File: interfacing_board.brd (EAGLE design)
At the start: 85.1 x 74.6 mm, 46 parts, among them IC1 MAX3096CSE, X1 87758-3816, X2 87758-3816

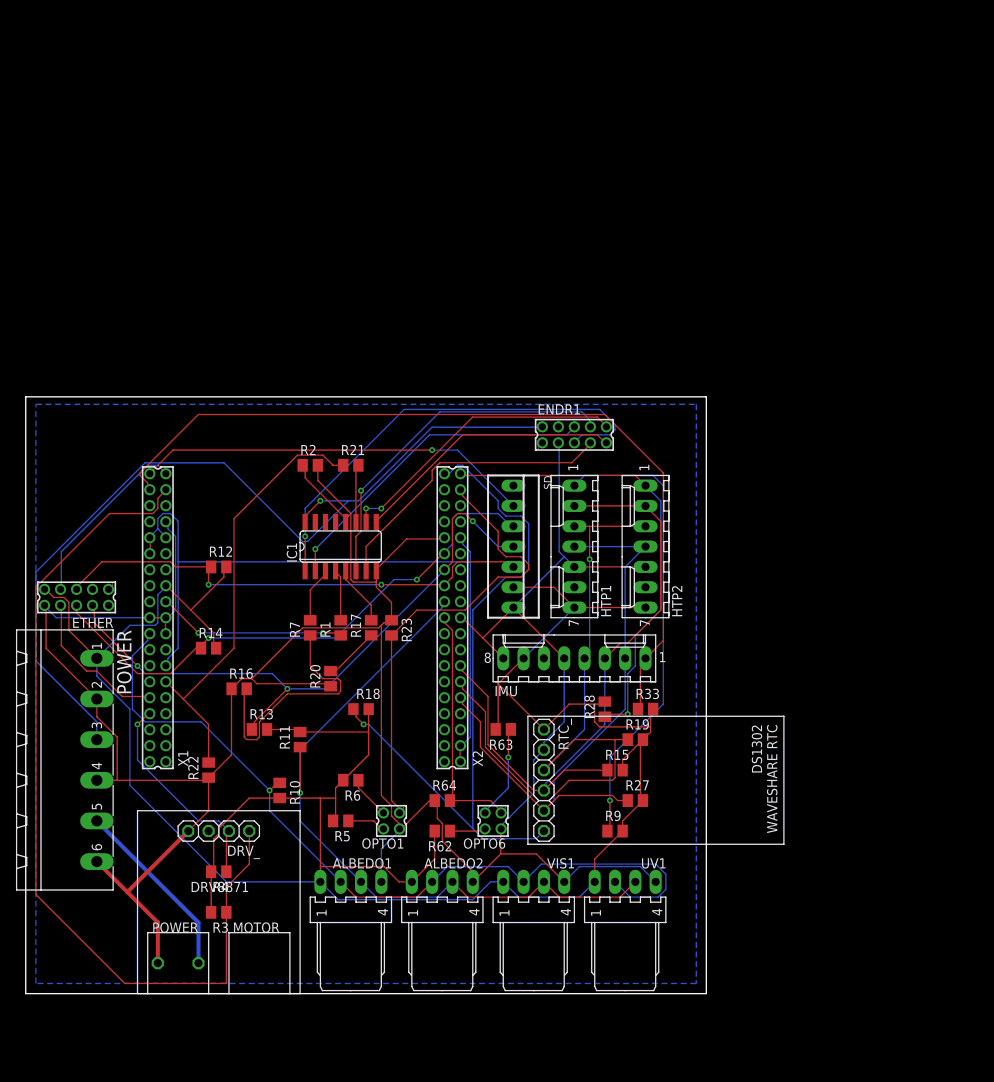
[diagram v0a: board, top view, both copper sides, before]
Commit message: Nucleo and ethernet module library components added. Implemented in schematics and PCB. Redesign of the PCB, errors removal.
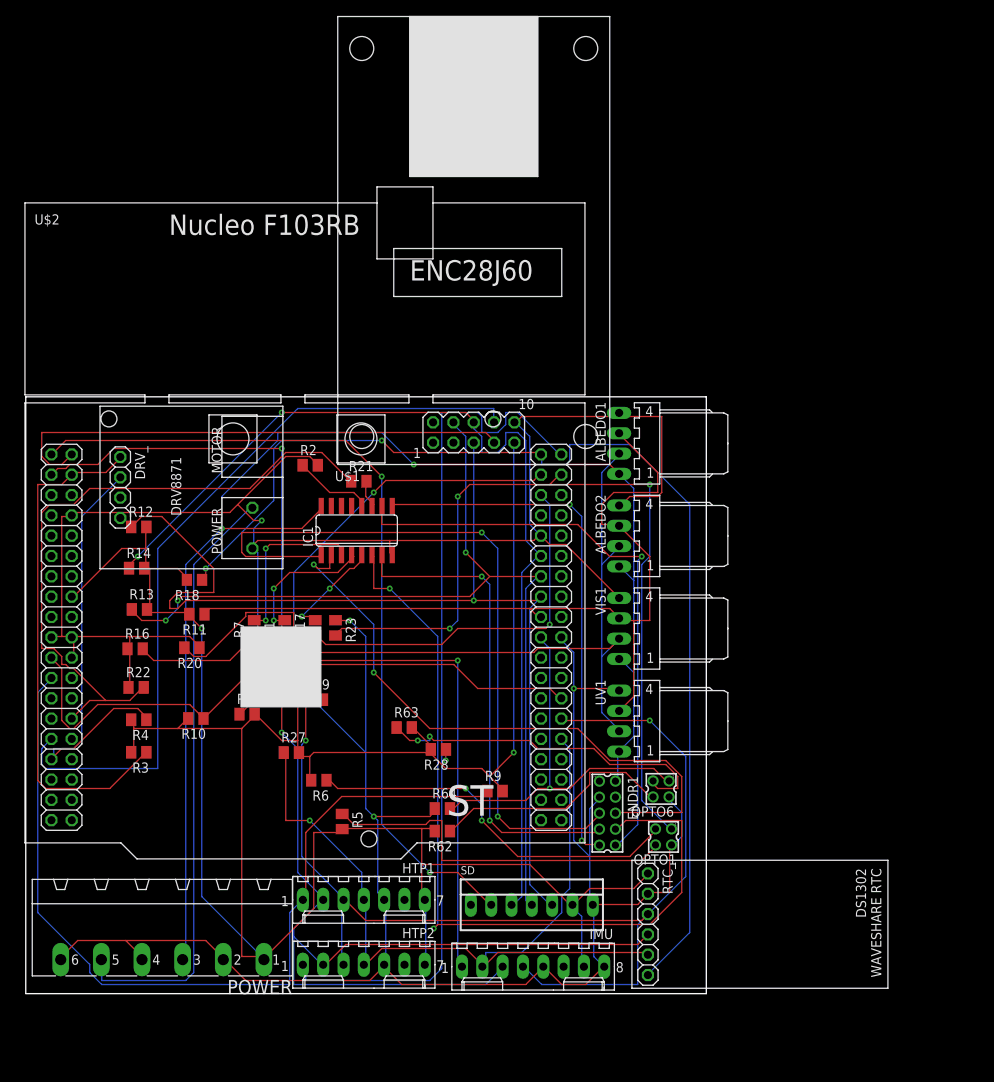
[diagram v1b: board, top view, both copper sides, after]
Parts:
- removed ETHER: 332-10, con-garry:332-10
- removed X1, X2: 87758-3816, con-molex:87758-3816
- added U$1: ETHERNET, customy:ETHERNET
- added U$2: NUCLEOF103, customy:NUCLEO
- moved ALBEDO1 64.3 mm to (74.2, 91.6), turned to 270 degrees
- moved HTP2 63.0 mm to (42.3, 26.5), turned to 180 degrees
- moved HTP1 51.4 mm to (42.3, 34.6), turned to 180 degrees
- moved ALBEDO2 48.6 mm to (74.2, 80.1), turned to 270 degrees
- moved ENDR1 47.5 mm to (72.7, 45.4), turned to 270 degrees
- moved R15 46.5 mm to (27.7, 57.8)
- moved R33 45.2 mm to (32.5, 62.4)
- moved SD 44.8 mm to (63.3, 34.0), turned to 0 degrees
- moved R27 43.4 mm to (33.2, 53.0)
- moved DRV_ 41.6 mm to (11.8, 83.6), turned to 270 degrees
- moved R19 40.3 mm to (36.2, 59.6)
- moved IMU 38.9 mm to (63.4, 26.2), turned to 180 degrees
- moved OPTO1 34.1 mm to (79.7, 42.5)
- moved VIS1 33.4 mm to (74.2, 68.5), turned to 270 degrees
- moved R18 26.4 mm to (21.1, 74.6), turned to 180 degrees
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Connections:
- removed net ADC12_IN8: X1.5
- removed net ADC12_IN9: X1.3
- removed net AGND: X2.7
- removed net AVDD: X2.32
- removed net BOOT0: X1.32
- removed net E5V: X1.33
- removed net INT: ETHER.2
- removed net IOREF: X1.27
- removed net NC: X1.13, X1.28, X1.29, X1.30, X2.1, X2.29, X2.3
- removed net PA1: X1.9
- removed net PA10: X2.6
- removed net PA11: X2.25
- removed net PA12: X2.27
- removed net PA13: X1.26
- removed net PA14: X1.24
- removed net PA15: X1.22
- removed net PA2: X2.4
- removed net PA3: X2.2
- removed net PA8: X2.16
- removed net PA9: X2.18
- removed net PB1: X2.15
- removed net PB10: X2.14
- removed net PB11: X2.21
- removed net PB12: X2.23
- removed net PB2: X2.17
- removed net PB3: X2.8
- removed net PB4: X2.12
- removed net PB5: X2.10
- removed net PB8: X2.36
- removed net PB9: X2.34
- removed net PC0: X1.1
- removed net PC13: X1.16
- removed net PC14: X1.14
- removed net PC15: X1.12
- removed net PC2: X1.4
- removed net PC3: X1.2
- removed net PC4: X2.5
- removed net PC5: X2.33
- removed net RESET: X1.25
- removed net SPI1_NSS: X1.7
- removed net U5V: X2.31
- removed net VBAT: X1.6
- removed net VDD: X1.34
- removed net VIN: X1.15
- new net ETH_INT: U$1.INT
- new net N$17: U$2.PC5
- new net N$20: U$2.PC4
- new net N$21: U$2.PC3
- new net N$22: U$2.PC2
- new net N$23: U$2.PC1
- new net N$24: U$2.PC0
- new net N$28: U$2.RESET
- new net N$29: U$2.BOOT0
- new net N$3: U$2.PC15
- new net N$30: U$2.IOREF
- new net N$34: U$2.PA1
- new net N$35: U$2.PA2
- new net N$36: U$2.PA3
- new net N$37: U$2.PA4
- new net N$4: U$1.WOL
- new net N$41: U$2.PA8
- new net N$42: U$2.PA9
- new net N$43: U$2.PA10
- new net N$44: U$2.PA11
- new net N$45: U$2.PA12
- new net N$46: U$2.PA13
- new net N$47: U$2.PA14
- new net N$48: U$2.PA15
- new net N$49: U$2.PB0
- new net N$5: U$2.PC14
- new net N$50: U$2.PB1
- new net N$51: U$2.PB2
- new net N$52: U$2.PB3
- new net N$53: U$2.PB4
- new net N$54: U$2.PB5
- new net N$59: U$2.PB10
- new net N$60: U$2.PB11
- new net N$61: U$2.PB12
- net +5V: no longer X1.21
- net 3.3V: now also U$1.VCC, U$2.3V3; no longer ALBEDO1.1, ALBEDO2.1, ETHER.9, UV1.1, VIS1.1, X1.23
- net 5V: now also ALBEDO1.1, ALBEDO2.1, UV1.1, VIS1.1
- net CHA-1L: now also U$2.PB8
- net CHB-1L: now also U$2.PB9
- net CHC-1L: now also U$2.PA0; no longer X1.11
- net CLKOUT: now also U$1.CLKOUT; no longer ETHER.1
- net CS_ETH: now also U$1.CS, U$2.PC11; no longer ETHER.7, X1.37
- net CS_HTP: now also U$2.PC13
- net CS_HTP2: now also U$2.PC8; no longer X2.37
- net CS_IMU: now also U$2.PC12; no longer X1.36
- net CS_RTC: now also U$2.PC9; no longer X2.38
- net CS_SD: now also U$2.PC10; no longer X1.38
- net ETH_RES: now also U$1.RESET, U$2.PD0; no longer ETHER.8, X1.10
- net GND: now also U$1.GND, U$2.GND, U$2.GND1, U$2.GND2, U$2.GND3, U$2.GND5, U$2.GND6; no longer ETHER.10, X1.17, X1.19, X1.20, X1.31, X2.19, X2.30
- net IND1: now also U$2.PC6; no longer X2.35
- net IND2: now also U$2.PC7; no longer X2.20
- net M11: now also U$2.PD1; no longer X1.8
- net M12: now also U$2.PD2; no longer X1.35
- net SCL1: now also U$2.PB6; no longer X2.22
- net SDA1: now also U$2.PB7; no longer X1.18
- net SPI1_MISO: now also U$1.SO, U$2.PA6; no longer ETHER.4, X2.26
- net SPI1_MOSI: now also U$1.SI, U$2.PA7; no longer ETHER.5, X2.24
- net SPI1_SCK: now also U$1.SCK, U$2.PA5; no longer ETHER.6, X2.28
- net SPI2_MISO: now also U$2.PB14; no longer X2.11
- net SPI2_MOSI: now also U$2.PB15; no longer X2.13
- net SPI2_SCK: now also U$2.PB13; no longer X2.9
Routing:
- net NC: track 93.8 -> 0.00 mm
- net GND: track 350.9 -> 436.4 mm, vias 0 -> 4
- net SPI2_MOSI: track 81.6 -> 161.0 mm, vias 0 -> 1
- net ETH_RES: track 18.8 -> 96.9 mm
- net SPI1_MOSI: track 61.3 -> 130.6 mm, vias 2 -> 1
- net 5V: track 110.0 -> 174.7 mm, vias 1 -> 2
- net CHB-1L: track 6.93 -> 69.5 mm, vias 0 -> 1
- net INCHB-1: track 44.3 -> 102.1 mm, vias 1 -> 2
- net CS_SD: track 49.6 -> 105.2 mm, vias 1 -> 2
- net SPI1_SCK: track 69.9 -> 124.7 mm
- net CS_HTP2: track 58.0 -> 112.5 mm
- net 12V: track 23.0 -> 75.8 mm
- net CS_RTC: track 88.1 -> 140.7 mm, vias 1 -> 2
- net CS_HTP: track 58.4 -> 110.5 mm, vias 1 -> 0
- net SPI2_MISO: track 88.2 -> 139.3 mm, vias 1 -> 2
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- removed copper zone on layer 16, net GND

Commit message: BIPOP board redesigned, new versions of transducers added.
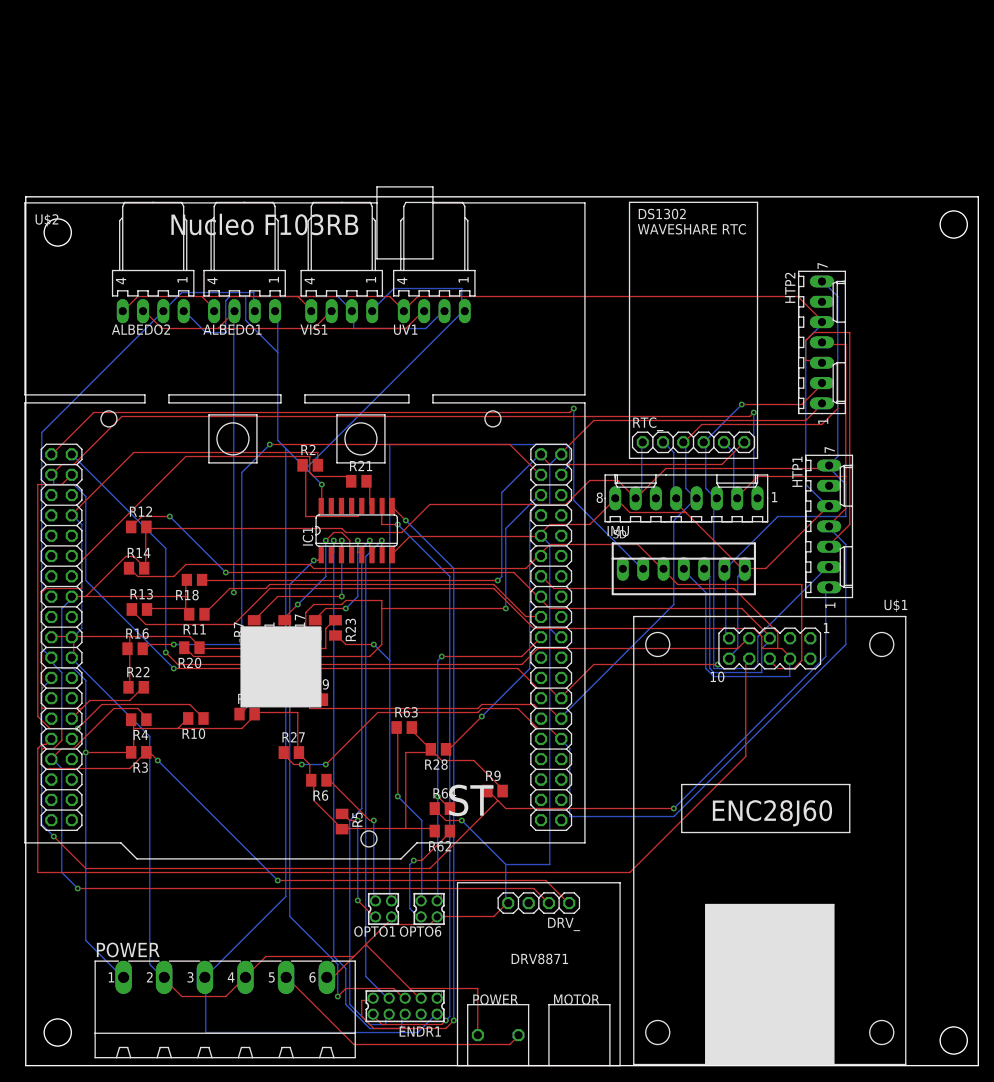
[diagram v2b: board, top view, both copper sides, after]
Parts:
- moved HTP2 96.6 mm to (99.5, 104.3), turned to 270 degrees
- moved HTP1 74.6 mm to (100.4, 81.3), turned to 270 degrees
- moved U$1 73.5 mm to (110.0, 70.0), turned to 180 degrees
- moved DRV_ 70.1 mm to (61.6, 34.2), turned to 180 degrees
- moved ALBEDO2 64.7 mm to (15.9, 108.2), turned to 0 degrees
- moved IMU 61.6 mm to (82.6, 84.8), turned to 0 degrees
- moved RTC_ 60.5 mm to (83.5, 91.8), turned to 0 degrees
- moved UV1 56.2 mm to (51.1, 108.2), turned to 0 degrees
- moved VIS1 52.7 mm to (39.5, 108.2), turned to 0 degrees
- moved ALBEDO1 49.6 mm to (27.4, 108.2), turned to 0 degrees
- moved SD 46.1 mm to (82.3, 76.0)
- moved OPTO1 36.1 mm to (44.7, 33.5)
- moved ENDR1 35.0 mm to (47.4, 21.3), turned to 180 degrees
- moved OPTO6 32.6 mm to (50.4, 33.5)
- moved POWER 14.7 mm to (24.9, 19.8), turned to 0 degrees
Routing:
- net GND: track 436.4 -> 497.8 mm, vias 4 -> 1
- net CS_RTC: track 140.7 -> 82.2 mm, vias 2 -> 1
- net M12: track 64.6 -> 118.5 mm, vias 0 -> 2
- net SPI2_SCK: track 107.0 -> 158.1 mm, vias 1 -> 2
- net 12V: track 75.8 -> 33.0 mm
- net CS_ETH: track 64.9 -> 104.5 mm, vias 0 -> 1
- net M11: track 55.5 -> 92.5 mm, vias 0 -> 1
- net INCHB-1: track 102.1 -> 68.0 mm, vias 2 -> 1
- net CS_HTP2: track 112.5 -> 79.3 mm
- net SPI1_MISO: track 118.3 -> 150.8 mm, vias 3 -> 0
- net CS_HTP: track 110.5 -> 141.6 mm, vias 0 -> 2
- net N$7: track 45.8 -> 15.3 mm, vias 0 -> 2
- net N$2: track 47.8 -> 18.2 mm, vias 2 -> 1
- net CS_IMU: track 119.6 -> 147.6 mm, vias 3 -> 2
- net ETH_RES: track 96.9 -> 124.7 mm
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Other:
- board size 85.1 x 74.6 mm -> 119.1 x 108.6 mm

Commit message: Further footprint updates, BIPOP v. 1.8 ready to order.
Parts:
- removed ENDR1: 332-10, con-garry:332-10
- removed OPTO6: 332-04, con-garry:332-04
- added OPTO2: (no value), pinhead:2X02
- added R24, R8: (no value), resistor:M0805
- added U$3: ENX10, customy:SIL25
- ALBEDO1, ALBEDO2, UV1, VIS1: value 22-05-7048-04 -> 22-27-2041-04; device EP_molex_6410_7395:7395-04 -> EP_molex_6410_7395:6410-04
- OPTO1: value 332-04 -> (none); device con-garry:332-04 -> pinhead:2X02
- SD: value 22-23-2071 -> SD_2597; device con-molex:22-23-2071 -> customy:SD
- moved ALBEDO2 95.2 mm to (109.0, 88.0), turned to 90 degrees
- moved ALBEDO1 87.4 mm to (109.0, 77.0), turned to 90 degrees
- moved VIS1 70.1 mm to (109.0, 99.0), turned to 90 degrees
- moved UV1 58.0 mm to (109.0, 110.0), turned to 90 degrees
- moved R3 56.4 mm to (69.0, 39.9), turned to 90 degrees
- moved R4 54.8 mm to (66.1, 39.9), turned to 90 degrees
- moved R15 50.3 mm to (77.8, 61.3), turned to 270 degrees
- moved R9 48.7 mm to (12.8, 64.7), turned to 90 degrees
- moved R18 48.0 mm to (64.6, 94.9), turned to 90 degrees
- moved R13 47.2 mm to (61.1, 76.2), turned to 90 degrees
- moved R14 46.4 mm to (60.1, 80.0), turned to 180 degrees
- moved R12 45.0 mm to (58.8, 76.1), turned to 90 degrees
- moved R28 44.3 mm to (68.4, 94.4), turned to 90 degrees
- moved R33 41.4 mm to (7.47, 95.4)
- moved R27 41.1 mm to (74.0, 58.2), turned to 90 degrees
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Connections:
- net N$18 renamed REC_PULLUP
- net N$19 renamed REC_PULLDOWN
- removed net +5V: R1.1
- new net ~INCHC1: U$3.!CHC
- net 3.3V: now also ALBEDO1.1, ALBEDO2.1, R24.2, R8.2, SD.VDD2, UV1.1, VIS1.1; no longer SD.6
- net 5V: now also R1.1, U$3.VCC; no longer ALBEDO1.1, ALBEDO2.1, ENDR1.2, UV1.1, VIS1.1
- net CD_SD: now also SD.DETECT; no longer SD.1
- net CS_ETH: now also R24.1
- net CS_SD: now also R8.1, SD.CS; no longer SD.2
- net GND: now also OPTO1.3, OPTO2.3, SD.GND2, U$3.GND; no longer ENDR1.3, OPTO1.2, OPTO6.2, SD.7
- net INCHA-1: now also U$3.CHA; no longer ENDR1.6
- net INCHB-1: now also U$3.CHB; no longer ENDR1.8
- net INCHC-1: now also U$3.CHC; no longer ENDR1.10
- net IND1: now also OPTO1.4; no longer OPTO1.1
- net IND2: now also OPTO2.4; no longer OPTO6.1
- net N$12: now also OPTO2.2; no longer OPTO6.3
- net N$15: now also OPTO2.1; no longer OPTO6.4
- net N$2: now also OPTO1.2; no longer OPTO1.3
- net N$7: now also OPTO1.1; no longer OPTO1.4
- net SPI1_MISO: now also SD.DO; no longer SD.4
- net SPI1_MOSI: now also SD.DI; no longer SD.5
- net SPI1_SCK: now also SD.SCLK; no longer SD.3
- net ~INCHA-1: now also U$3.!CHA; no longer ENDR1.5
- net ~INCHB-1: now also U$3.!CHB; no longer ENDR1.7
- net ~INCHC-1: no longer ENDR1.9
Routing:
- net 5V: track 199.0 -> 86.8 mm, vias 1 -> 4
- net SPI1_MISO: track 150.8 -> 63.3 mm, vias 0 -> 2
- net ~INCHC-1: track 83.5 -> 0.00 mm, vias 2 -> 0
- net SDA1: track 121.4 -> 202.8 mm, vias 1 -> 3
- net 3.3V: track 348.6 -> 422.3 mm, vias 1 -> 8
- net CS_IMU: track 147.6 -> 92.1 mm, vias 2 -> 0
- net SPI1_MOSI: track 111.1 -> 56.4 mm, vias 2 -> 3
- net CS_HTP: track 141.6 -> 193.4 mm, vias 2 -> 6
- net INCHC-1: track 79.1 -> 27.8 mm
- net ~INCHA-1: track 68.9 -> 19.5 mm, vias 2 -> 0
- net INCHA-1: track 70.8 -> 24.3 mm
- net CS_RTC: track 82.2 -> 36.5 mm, vias 1 -> 0
- net ~INCHB-1: track 61.2 -> 18.1 mm, vias 1 -> 0
- net INCHB-1: track 68.0 -> 25.9 mm, vias 1 -> 0
- net SPI1_SCK: track 103.4 -> 61.8 mm
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- added copper zone on layer 16, net GND

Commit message: poprawione routowanie
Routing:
- net CS_HTP: track 193.4 -> 179.6 mm
- net SDA1: track 202.8 -> 196.4 mm
- net SPI1_SCK: track 61.8 -> 55.9 mm
- net SPI1_MISO: track 63.3 -> 57.6 mm
- net CS_ETH: track 137.5 -> 131.9 mm
- net INCHA-1: track 24.3 -> 19.3 mm
- net SPI2_SCK: track 126.1 -> 121.5 mm
- net M11: track 85.1 -> 80.6 mm
- net ETH_RES: track 160.0 -> 155.6 mm
- net CS_SD: track 113.2 -> 109.4 mm
- net GND: track 460.4 -> 463.6 mm
- net M12: track 106.9 -> 104.8 mm
- net SPI2_MISO: track 115.6 -> 113.6 mm
- net CHC-1L: track 64.6 -> 62.8 mm
- net CS_RTC: track 36.5 -> 34.7 mm
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
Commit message: refit
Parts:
- removed DRV_: DRV8871, customy:DRIVER
- removed RTC_: RTC_WAVESHARE, SKA_EP_molex_6410_7395:RTC
- added JP16: RTC_WAVESHARE, customy:RTC
- added JP4: DRV8871, customy:DRIVER
- JP1A: value NUCLEOF103 -> JP1B
- R10, R11, R18, R28, R33, R9: value 4.7k -> 2k49
- R12, R13, R14, R15, R19, R27: value 5k -> 2k49
- R16, R20, R22: value 10k -> 20k
- R17, R21, R7: value 5k -> 10k
- R23, R64: value (none) -> 47k
- R24, R8: value (none) -> 2k49
- R5, R62: value (none) -> 82k
- R6, R63: value (none) -> 5k
- renumbered ALBEDO1 to JP7, ALBEDO2 to JP8, HTP1 to JP10, HTP2 to JP11, IMU to JP3, OPTO1 to JP13, OPTO2 to JP14, POWER to JP9, SD to JP12, U$1 to JP2, U$2 to JP1A, U$3 to JP15, UV1 to JP5, VIS1 to JP6
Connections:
- removed net N$17: JP1A.PC5
- removed net N$20: JP1A.PC4
- removed net N$21: JP1A.PC3
- removed net N$22: JP1A.PC2
- removed net N$23: JP1A.PC1
- removed net N$24: JP1A.PC0
- removed net N$3: JP1A.PC15
- removed net N$34: JP1A.PA1
- removed net N$35: JP1A.PA2
- removed net N$36: JP1A.PA3
- removed net N$37: JP1A.PA4
- removed net N$41: JP1A.PA8
- removed net N$42: JP1A.PA9
- removed net N$43: JP1A.PA10
- removed net N$44: JP1A.PA11
- removed net N$45: JP1A.PA12
- removed net N$46: JP1A.PA13
- removed net N$47: JP1A.PA14
- removed net N$48: JP1A.PA15
- removed net N$49: JP1A.PB0
- removed net N$5: JP1A.PC14
- removed net N$50: JP1A.PB1
- removed net N$51: JP1A.PB2
- removed net N$52: JP1A.PB3
- removed net N$53: JP1A.PB4
- removed net N$54: JP1A.PB5
- removed net N$59: JP1A.PB10
- removed net N$60: JP1A.PB11
- removed net N$61: JP1A.PB12
- net 12V: now also JP4.MOTOR_VCC; no longer DRV_.MOTOR_VCC
- net 3.3V: now also JP16.VCC; no longer RTC_.VCC
- net CS_RTC: now also JP16.CS; no longer RTC_.CS
- net DRV1-VM: now also JP4.VM; no longer DRV_.VM
- net GND: now also JP16.GND, JP4.GND, JP4.MOTOR_GND; no longer DRV_.GND, DRV_.MOTOR_GND, RTC_.GND
- net M11: now also JP4.IN1; no longer DRV_.IN1
- net M12: now also JP4.IN2; no longer DRV_.IN2
- net SPI2_MISO: now also JP16.MISO; no longer RTC_.MISO
- net SPI2_MOSI: now also JP16.MOSI; no longer RTC_.MOSI
- net SPI2_SCK: now also JP16.SCK; no longer RTC_.SCK
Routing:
- net GND: track 463.6 -> 460.8 mm
